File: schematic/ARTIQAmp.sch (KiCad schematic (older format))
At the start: 2 parts, among them J1 HD68, J2 HD68

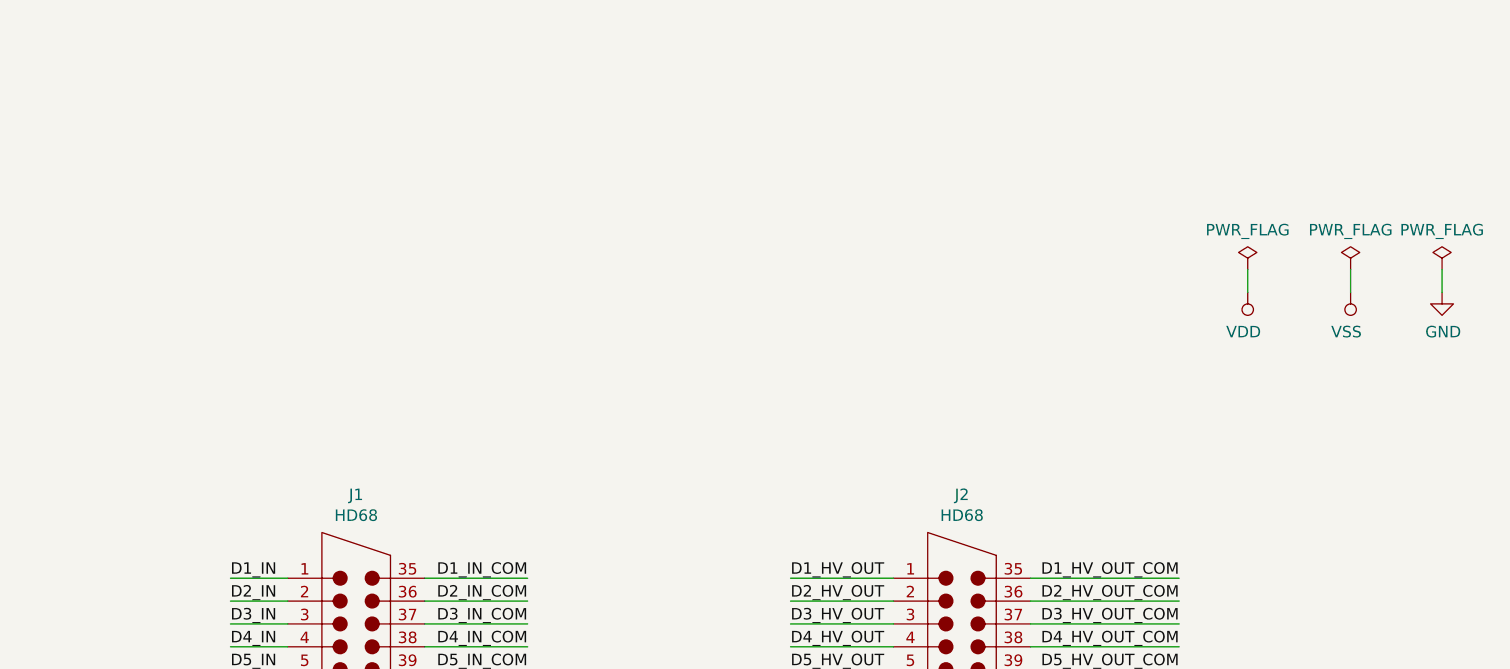
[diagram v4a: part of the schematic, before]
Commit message: Add power connections; assign footprints to all components
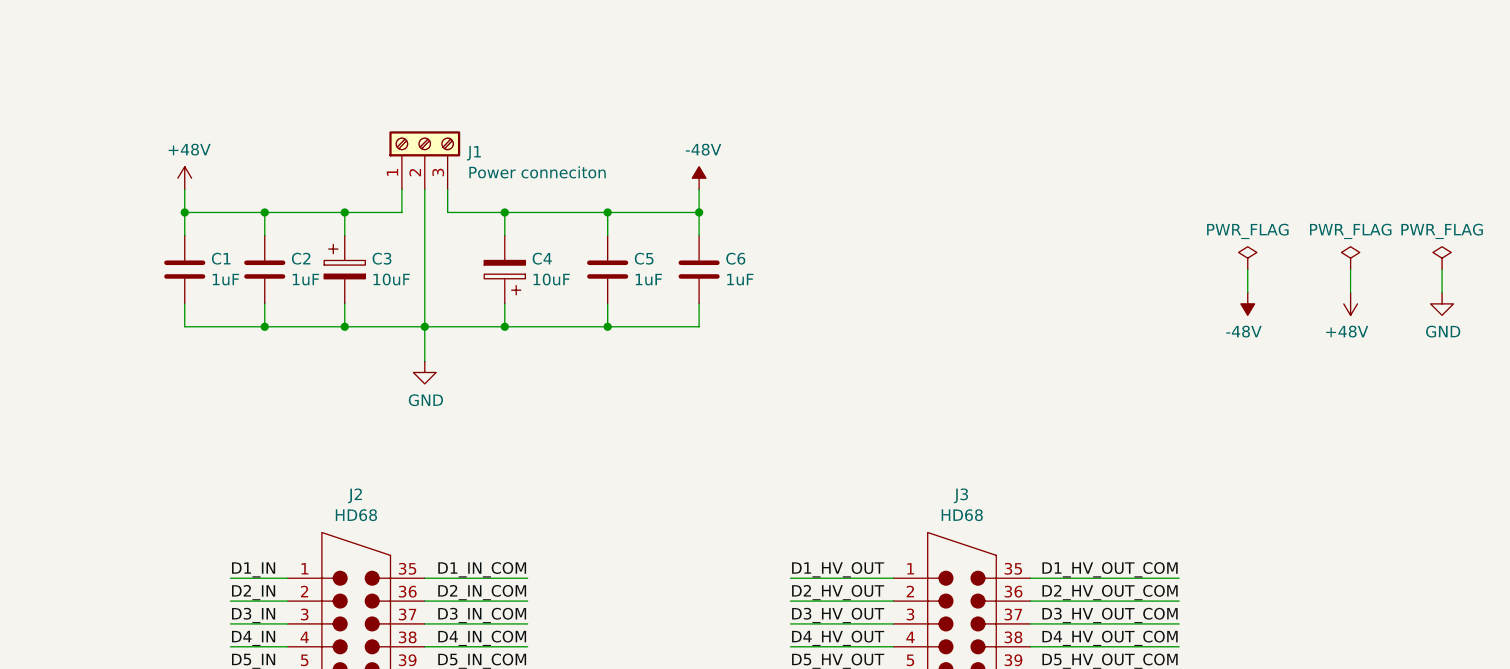
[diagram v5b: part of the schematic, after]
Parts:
- added C1, C2, C5, C6: 1uF, Capacitor_SMD:C_0603_1608Metric, symbol Device:C
- added C3, C4: 10uF, Capacitor_THT:CP_Radial_D6.3mm_P2.50mm, symbol Device:CP
- added J1: Power conneciton, TerminalBlock_Phoenix:TerminalBlock_Phoenix_PT-1,5-3-5.0-H_1x03_P5.00mm_Horizontal, symbol ARTIQAmp:Screw_Terminal_01x03
- J2: renamed from J1; footprint (none) -> ARTIQAmp:5787082-7_1
- J3: renamed from J2; footprint (none) -> ARTIQAmp:5787082-7_1
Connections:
- net GND: now also C1.2, C2.2, C3.2, C4.1, C5.2, C6.2, J1.2 (Pin_2)
- new net +48V: C1.1, C2.1, C3.1, J1.1 (Pin_1)
- new net -48V: C4.2, C5.1, C6.1, J1.3 (Pin_3)
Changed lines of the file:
@@
 ToDo:\n>Think about better ways to ground the sheild of the cables\n>Ground loops?!
 $Comp
-L ARTIQAmp:HD68 J1
+L ARTIQAmp:HD68 J2
 U 1 1 5C9B14C8
 P 9150 4900
-F 0 "J1" H 9150 6915 50  0000 C CNN
+F 0 "J2" H 9150 6915 50  0000 C CNN
 F 1 "HD68" H 9150 6824 50  0000 C CNN
-F 2 "" H 9150 4750 50  0001 C CNN
+F 2 "ARTIQAmp:5787082-7_1" H 9150 4750 50  0001 C CNN
 F 3 " ~" H 9150 4750 50  0001 C CNN
 	1    9150 4900
@@
 	13050 1900 13050 2000
 $Comp
-L power:VDD #PWR05
+L power:-48V #PWR03
 U 1 1 5C985B3C
 P 13050 2000
-F 0 "#PWR05" H 13050 1850 50  0001 C CNN
-F 1 "VDD" H 13068 2173 50  0000 C CNN
+F 0 "#PWR03" H 13050 1850 50  0001 C CNN
+F 1 "-48V" H 13068 2173 50  0000 C CNN
 F 2 "" H 13050 2000 50  0001 C CNN
 F 3 "" H 13050 2000 50  0001 C CNN
@@
 $EndComp
 $Comp
-L power:VSS #PWR06
+L power:+48V #PWR04
 U 1 1 5C983C61
 P 13500 2000
-F 0 "#PWR06" H 13500 1850 50  0001 C CNN
-F 1 "VSS" H 13518 2173 50  0000 C CNN
+F 0 "#PWR04" H 13500 1850 50  0001 C CNN
+F 1 "+48V" H 13518 2173 50  0000 C CNN
 F 2 "" H 13500 2000 50  0001 C CNN
 F 3 "" H 13500 2000 50  0001 C CNN
@@
 $EndComp
 $Comp
-L power:GND #PWR07
+L power:GND #PWR05
 U 1 1 5C960B25
 P 13900 2000
-F 0 "#PWR07" H 13900 1750 50  0001 C CNN
+F 0 "#PWR05" H 13900 1750 50  0001 C CNN
 F 1 "GND" H 13905 1827 50  0000 C CNN
 F 2 "" H 13900 2000 50  0001 C CNN
@@
 	11500 3250 11050 3250
 $Comp
-L ARTIQAmp:HD68 J2
+L ARTIQAmp:HD68 J3
 U 1 1 5CB2EEB2
 P 11800 4900
-F 0 "J2" H 11800 6915 50  0000 C CNN
+F 0 "J3" H 11800 6915 50  0000 C CNN
 F 1 "HD68" H 11800 6824 50  0000 C CNN
-F 2 "" H 11800 4750 50  0001 C CNN
+F 2 "ARTIQAmp:5787082-7_1" H 11800 4750 50  0001 C CNN
 F 3 " ~" H 11800 4750 50  0001 C CNN
 	1    11800 4900
@@
 $EndComp
 $Comp
-L power:GND #PWR01
+L power:GND #PWR07
 U 1 1 5CB5B503
 P 8400 5050
-F 0 "#PWR01" H 8400 4800 50  0001 C CNN
+F 0 "#PWR07" H 8400 4800 50  0001 C CNN
 F 1 "GND" H 8405 4877 50  0000 C CNN
 F 2 "" H 8400 5050 50  0001 C CNN
@@
 $EndComp
 $Comp
-L power:GND #PWR02
+L power:GND #PWR08
 U 1 1 5CB5BA4F
 P 10100 5050
-F 0 "#PWR02" H 10100 4800 50  0001 C CNN
+F 0 "#PWR08" H 10100 4800 50  0001 C CNN
 F 1 "GND" H 10105 4877 50  0000 C CNN
 F 2 "" H 10100 5050 50  0001 C CNN
@@
 $EndComp
 $Comp
-L power:GND #PWR03
+L power:GND #PWR09
 U 1 1 5CB7F37C
 P 10850 5050
-F 0 "#PWR03" H 10850 4800 50  0001 C CNN
+F 0 "#PWR09" H 10850 4800 50  0001 C CNN
 F 1 "GND" H 10855 4877 50  0000 C CNN
 F 2 "" H 10850 5050 50  0001 C CNN
@@
 $EndComp
 $Comp
-L power:GND #PWR04
+L power:GND #PWR010
 U 1 1 5CB7F6F2
 P 12950 5050
-F 0 "#PWR04" H 12950 4800 50  0001 C CNN
+F 0 "#PWR010" H 12950 4800 50  0001 C CNN
 F 1 "GND" H 12955 4877 50  0000 C CNN
 F 2 "" H 12950 5050 50  0001 C CNN
@@
 NoConn ~ 9900 4950
 NoConn ~ 8600 4950
+$Comp
+L Device:CP C3
+U 1 1 5E6DC485
+P 9100 1900
+F 0 "C3" H 9218 1946 50  0000 L CNN
+F 1 "10uF" H 9218 1855 50  0000 L CNN
+F 2 "Capacitor_THT:CP_Radial_D6.3mm_P2.50mm" H 9138 1750 50  0001 C CNN
+F 3 "~" H 9100 1900 50  0001 C CNN
+	1    9100 1900
+	1    0    0    -1
+$EndComp
+$Comp
+L Device:C C2
+U 1 1 5E6E715C
+P 8750 1900
+F 0 "C2" H 8865 1946 50  0000 L CNN
+F 1 "1uF" H 8865 1855 50  0000 L CNN
+F 2 "Capacitor_SMD:C_0603_1608Metric" H 8788 1750 50  0001 C CNN
+F 3 "~" H 8750 1900 50  0001 C CNN
+	1    8750 1900
+	1    0    0    -1
+$EndComp
+$Comp
+L Device:C C1
+U 1 1 5E76A403
+P 8400 1900
+F 0 "C1" H 8515 1946 50  0000 L CNN
+F 1 "1uF" H 8515 1855 50  0000 L CNN
+F 2 "Capacitor_SMD:C_0603_1608Metric" H 8438 1750 50  0001 C CNN
+F 3 "~" H 8400 1900 50  0001 C CNN
+	1    8400 1900
+	1    0    0    -1
+$EndComp
+$Comp
+L Device:CP C4
+U 1 1 5E76A957
+P 9800 1900
+F 0 "C4" H 9682 1854 50  0000 R CNN
+F 1 "10uF" H 9682 1945 50  0000 R CNN
+F 2 "Capacitor_THT:CP_Radial_D6.3mm_P2.50mm" H 9838 1750 50  0001 C CNN
+F 3 "~" H 9800 1900 50  0001 C CNN
+	1    9800 1900
+	-1   0    0    1
+$EndComp
+$Comp
+L Device:C C5
+U 1 1 5E76AFA1
+P 10250 1900
+F 0 "C5" H 10365 1946 50  0000 L CNN
+F 1 "1uF" H 10365 1855 50  0000 L CNN
+F 2 "Capacitor_SMD:C_0603_1608Metric" H 10288 1750 50  0001 C CNN
+F 3 "~" H 10250 1900 50  0001 C CNN
+	1    10250 1900
+	1    0    0    -1
+$EndComp
+$Comp
+L Device:C C6
+U 1 1 5E76B6E6
+P 10650 1900
+F 0 "C6" H 10765 1946 50  0000 L CNN
+F 1 "1uF" H 10765 1855 50  0000 L CNN
+F 2 "Capacitor_SMD:C_0603_1608Metric" H 10688 1750 50  0001 C CNN
+F 3 "~" H 10650 1900 50  0001 C CNN
+	1    10650 1900
+	1    0    0    -1
+$EndComp
+$Comp
+L ARTIQAmp:Screw_Terminal_01x03 J1
+U 1 1 5E76C8E2
+P 9450 1350
+F 0 "J1" V 9414 1162 50  0000 R CNN
+F 1 "Power conneciton" V 9323 1162 50  0000 R CNN
+F 2 "TerminalBlock_Phoenix:TerminalBlock_Phoenix_PT-1,5-3-5.0-H_1x03_P5.00mm_Horizontal" H 9450 1350 50  0001 C CNN
+F 3 "~" H 9450 1350 50  0001 C CNN
+	1    9450 1350
+	0    -1   -1   0
+$EndComp
+$Comp
+L power:-48V #PWR02
+U 1 1 5E7E3CD5
+P 10650 1550
+F 0 "#PWR02" H 10650 1400 50  0001 C CNN
+F 1 "-48V" H 10668 1723 50  0000 C CNN
+F 2 "" H 10650 1550 50  0001 C CNN
+F 3 "" H 10650 1550 50  0001 C CNN
+	1    10650 1550
+	1    0    0    -1
+$EndComp
+$Comp
+L power:+48V #PWR01
+U 1 1 5E7E434D
+P 8400 1550
+F 0 "#PWR01" H 8400 1400 50  0001 C CNN
+F 1 "+48V" H 8418 1723 50  0000 C CNN
+F 2 "" H 8400 1550 50  0001 C CNN
+F 3 "" H 8400 1550 50  0001 C CNN
+	1    8400 1550
+	1    0    0    -1
+$EndComp
+$Comp
+L power:GND #PWR06
+U 1 1 5E7E4911
+P 9450 2300
+F 0 "#PWR06" H 9450 2050 50  0001 C CNN
+F 1 "GND" H 9455 2127 50  0000 C CNN
+F 2 "" H 9450 2300 50  0001 C CNN
+F 3 "" H 9450 2300 50  0001 C CNN
+	1    9450 2300
+	1    0    0    -1
+$EndComp
+Wire Wire Line
+	9450 1550 9450 2150
+Wire Wire Line
+	9350 1550 9350 1650
+Wire Wire Line
+	9350 1650 9100 1650
+Wire Wire Line
+	9100 1650 9100 1750
+Wire Wire Line
+	9100 1650 8750 1650
+Wire Wire Line
+	8750 1650 8750 1750
+Connection ~ 9100 1650
+Wire Wire Line
+	8750 1650 8400 1650
+Wire Wire Line
+	8400 1650 8400 1750
+Connection ~ 8750 1650
+Wire Wire Line
+	8400 1550 8400 1650
+Connection ~ 8400 1650
+Wire Wire Line
+	9550 1550 9550 1650
+Wire Wire Line
+	9550 1650 9800 1650
+Wire Wire Line
+	9800 1650 9800 1750
+Wire Wire Line
+	9800 1650 10250 1650
+Wire Wire Line
+	10250 1650 10250 1750
+Connection ~ 9800 1650
+Wire Wire Line
+	10250 1650 10650 1650
+Wire Wire Line
+	10650 1650 10650 1750
+Connection ~ 10250 1650
+Wire Wire Line
+	10650 1650 10650 1550
+Connection ~ 10650 1650
+Wire Wire Line
+	9100 2050 9100 2150
+Wire Wire Line
+	9100 2150 9450 2150
+Connection ~ 9450 2150
+Wire Wire Line
+	9450 2150 9450 2300
+Wire Wire Line
+	8750 2050 8750 2150
+Wire Wire Line
+	8750 2150 9100 2150
+Connection ~ 9100 2150
+Wire Wire Line
+	8400 2050 8400 2150
+Wire Wire Line
+	8400 2150 8750 2150
+Connection ~ 8750 2150
+Wire Wire Line
+	9800 2050 9800 2150
+Wire Wire Line
+	9800 2150 9450 2150
+Wire Wire Line
+	10250 2050 10250 2150
+Wire Wire Line
+	10250 2150 9800 2150
+Connection ~ 9800 2150
+Wire Wire Line
+	10650 2050 10650 2150
+Wire Wire Line
+	10650 2150 10250 2150
+Connection ~ 10250 2150
 $EndSCHEMATC

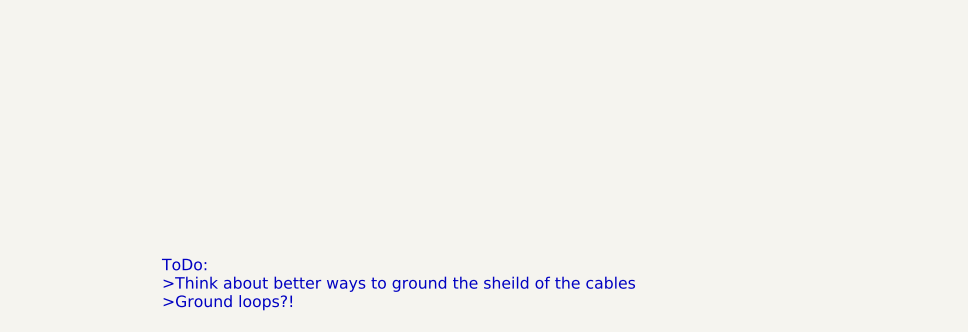
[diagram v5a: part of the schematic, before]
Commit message: finalize schematic and start organizing components in layout
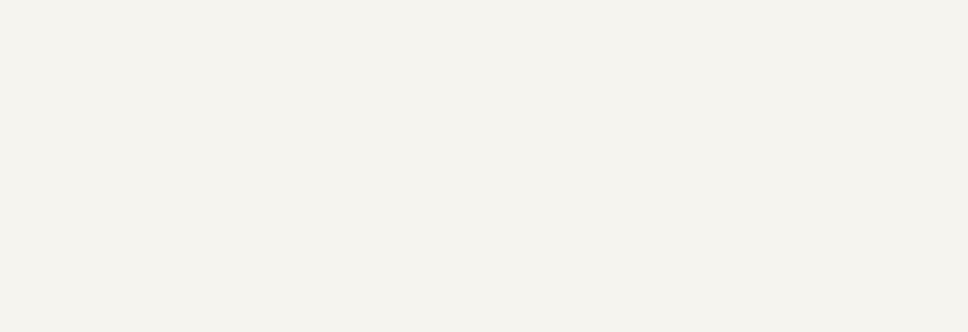
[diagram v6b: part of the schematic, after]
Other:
- note removed: "ToDo:\n>Think about better ways to ground the sheild of the cables\n>Ground loops?!"
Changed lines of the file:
@@
 Wire Wire Line
 	8850 3250 8600 3250
-Text Notes 10250 8900 0    50   ~ 0
-ToDo:\n>Think about better ways to ground the sheild of the cables\n>Ground loops?!
 $Comp
 L ARTIQAmp:HD68 J2
